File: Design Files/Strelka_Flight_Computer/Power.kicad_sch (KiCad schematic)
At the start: 12 parts

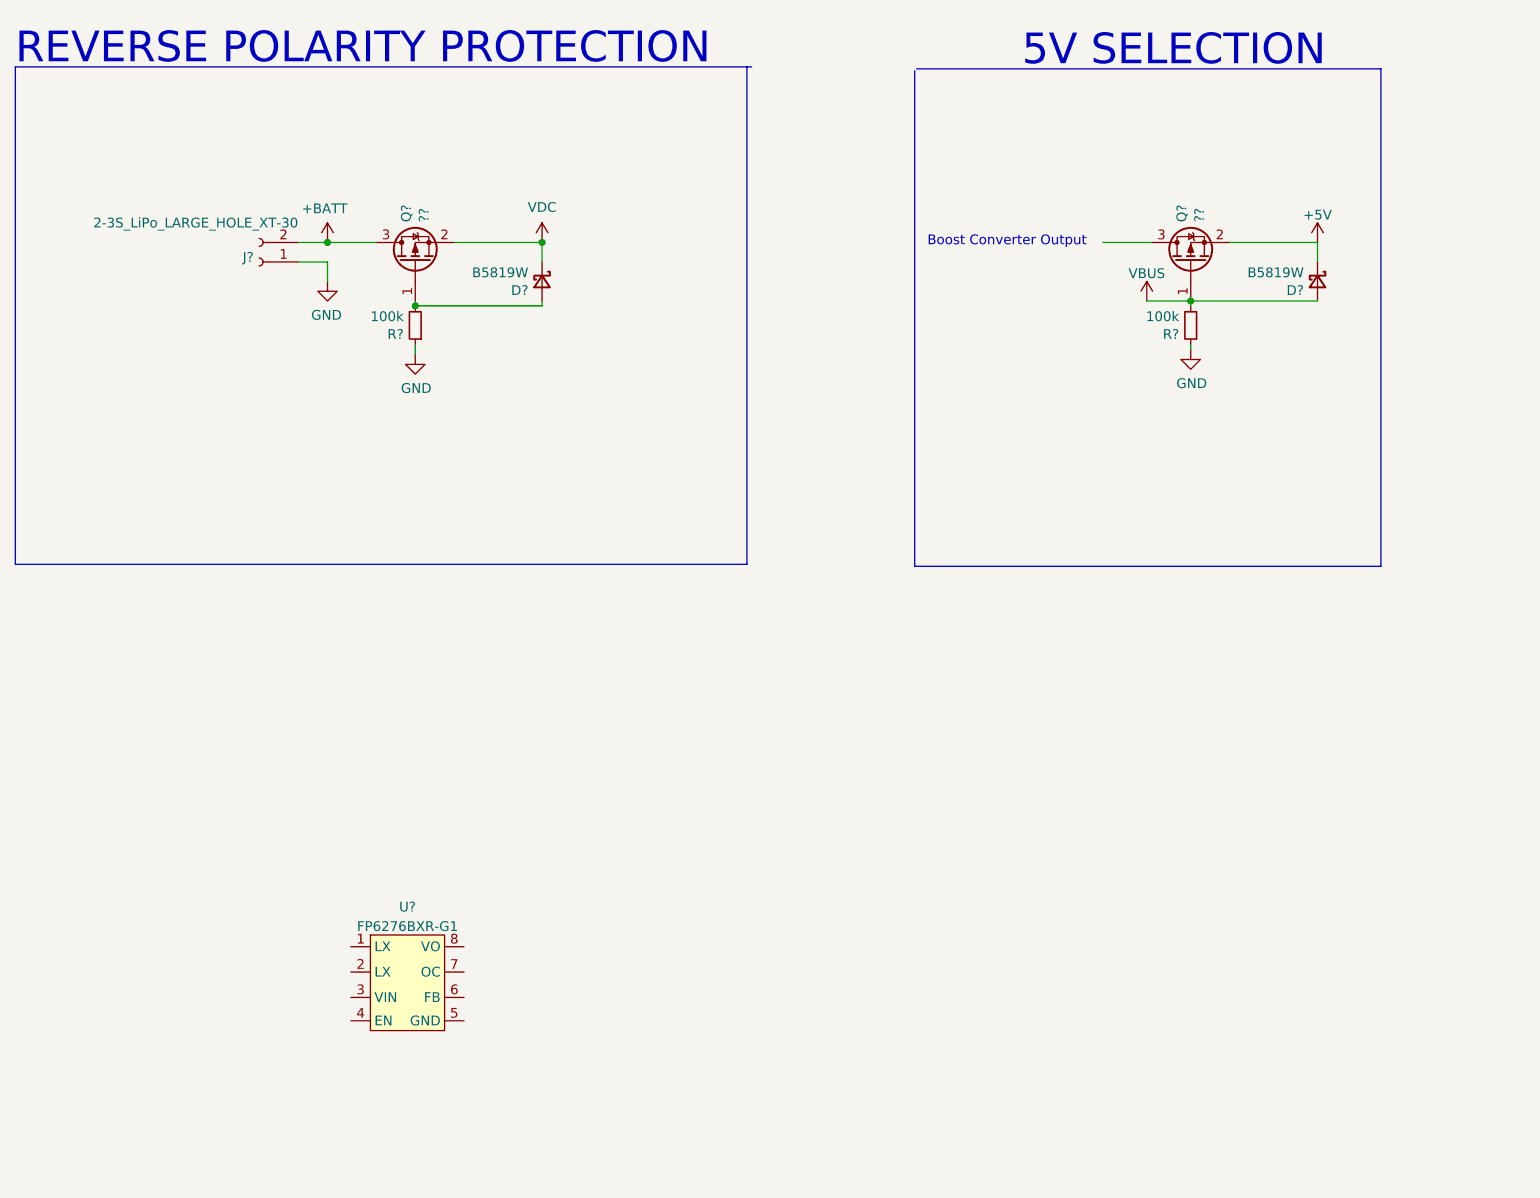
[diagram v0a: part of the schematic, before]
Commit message: Added boost converter
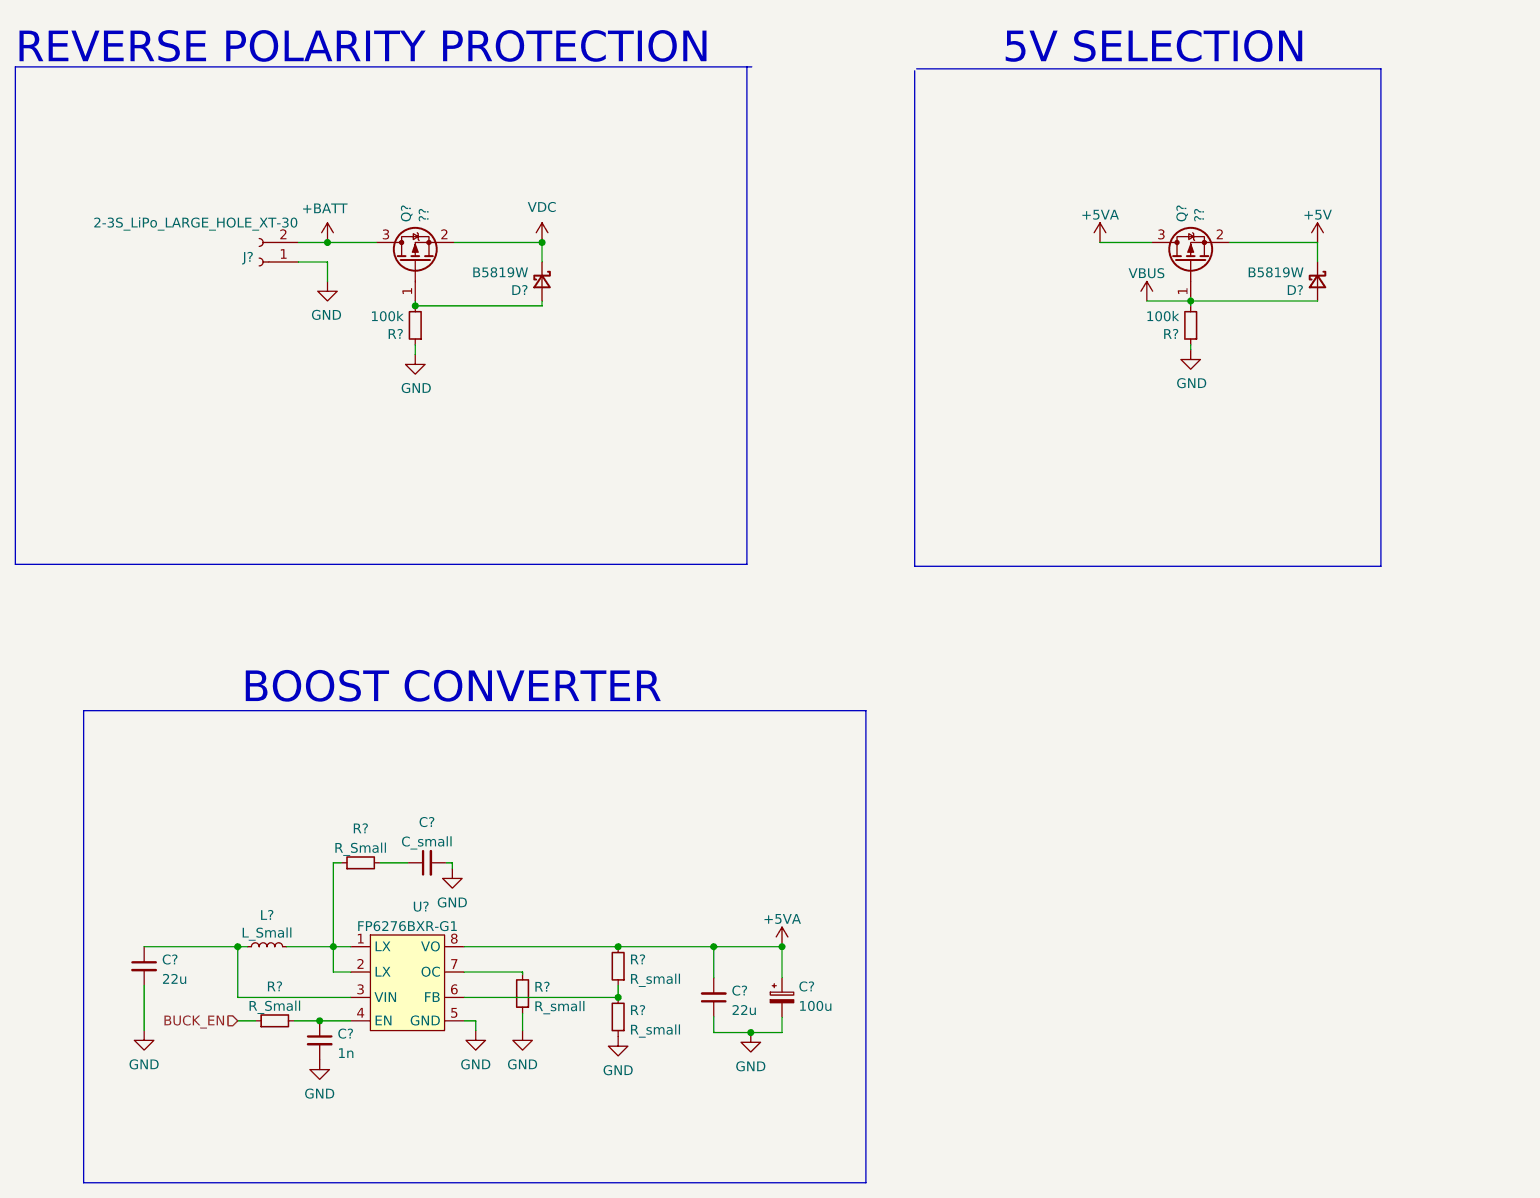
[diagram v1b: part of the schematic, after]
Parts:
- added C? (x2): 22u, symbol Device:C_Small
- added C?: 100u, symbol Device:C_Polarized_Small
- added C?: C_small, symbol Device:C_Small
- added C?: 1n, symbol Device:C_Small
- added L?: L_Small, symbol Device:L_Small
- added R? (x3): R_small, symbol Device:R_Small
- added R? (x2): R_Small, symbol Device:R_Small
- U?: footprint (none) -> Package_SO:Diodes_PSOP-8; LCSC# (none) -> C82652
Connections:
- net GND: now also U?.5 (GND), C?.1, C?.2, C?.2, C?.2, C?.2, R?.1, R?.1
- net +5VA: now reaches Q?.3 (D)
- net +5VA: now also U?.8 (VO), C?.1, C?.2, R?.2
- net at U?.1 (LX): now also U?.2 (LX), L?.2, R?.1
- net at U?.3 (VIN): now also C?.1, L?.1
- net at U?.4 (EN): now also C?.1, R?.2
- net at U?.6 (FB): now also R?.1, R?.2
- net at U?.7 (OC): now also R?.2
- new net: C?.1, R?.2
- new net BUCK_EN: R?.1
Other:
- note added: "BOOST CONVERTER"
- note removed: "Boost Converter Output"

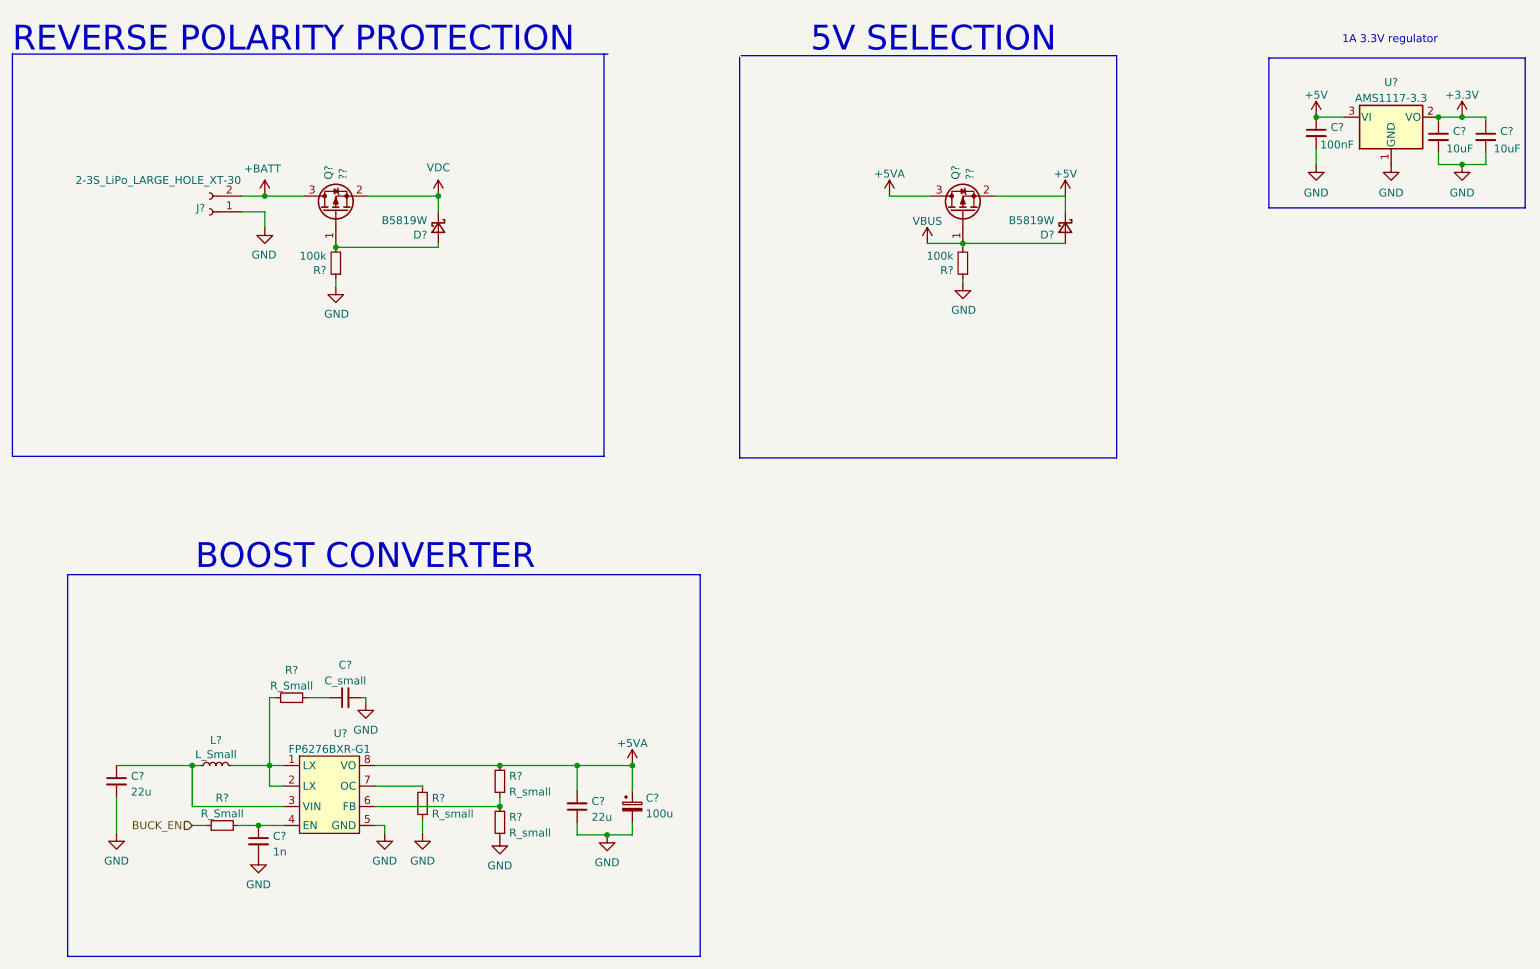
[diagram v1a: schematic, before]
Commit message: Working SPICE sim for ematch continuity circuit
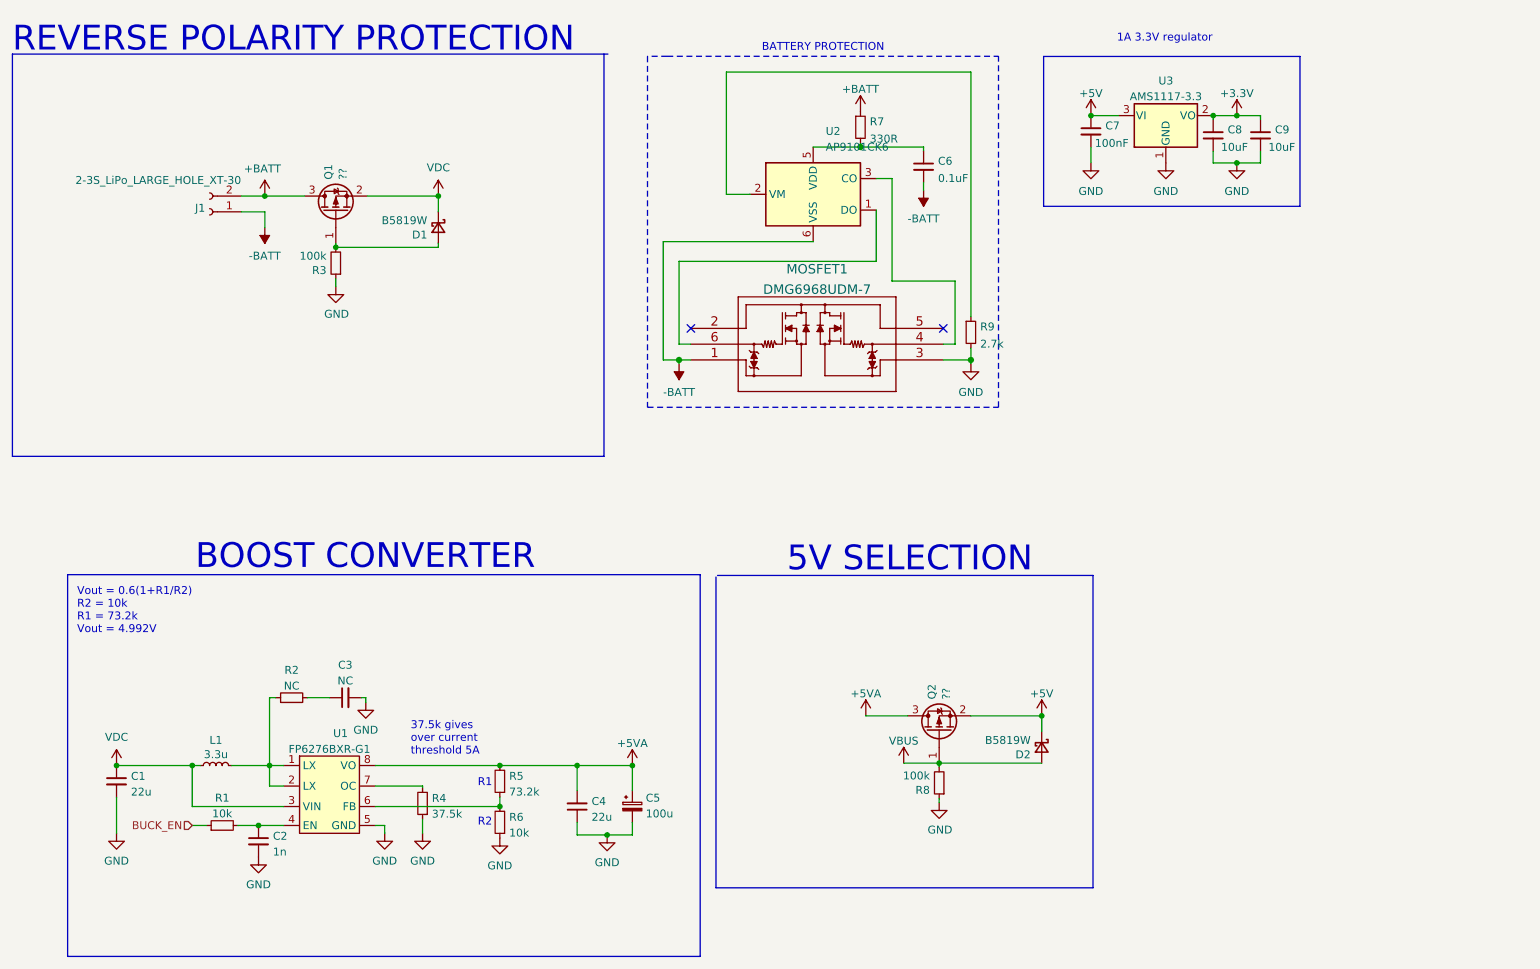
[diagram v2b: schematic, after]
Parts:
- added C6: 0.1uF, Capacitor_SMD:C_0603_1608Metric, symbol Device:C_Small
- added MOSFET1: DMG6968UDM-7, footprints:DMG6968UDM-7, symbol DMG6968UDM-7:DMG6968UDM-7
- added R7: 330R, Resistor_SMD:R_0603_1608Metric, symbol Device:R_Small
- added R9: 2.7k, Resistor_SMD:R_0603_1608Metric, symbol Device:R_Small
- added U2: AP9101CK6, Package_TO_SOT_SMD:SOT-23-6, symbol Battery_Management:AP9101CK6
- C1, C2, C4: renamed from C?; footprint (none) -> Capacitor_SMD:C_0603_1608Metric
- C3: renamed from C?; value C_small -> NC; footprint (none) -> Capacitor_SMD:C_0603_1608Metric
- L1: renamed from L?; value L_Small -> 3.3u; footprint (none) -> Inductor_SMD:L_Vishay_IHLP-2020; LCSC# (none) -> C553993
- R1: renamed from R?; value R_Small -> 10k; footprint (none) -> Resistor_SMD:R_0603_1608Metric
- R2: renamed from R?; value R_Small -> NC; footprint (none) -> Resistor_SMD:R_0603_1608Metric
- R4: renamed from R?; value R_small -> 37.5k; footprint (none) -> Resistor_SMD:R_0603_1608Metric
- R5: renamed from R?; value R_small -> 73.2k; footprint (none) -> Resistor_SMD:R_0603_1608Metric; LCSC# (none) -> C403343
- R6: renamed from R?; value R_small -> 10k; footprint (none) -> Resistor_SMD:R_0603_1608Metric
- gave numbers to parts that had none: 13
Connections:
- net +BATT: now also R7.1
- net GND: now also MOSFET1.3 (S2), R9.2; no longer J1.1 (Pin_1)
- net VDC: now also C1.1, L1.1, U1.3 (VIN)
- new net: MOSFET1.4 (G2), U2.3 (CO)
- new net: MOSFET1.6 (G1), U2.1 (DO)
- new net: R9.1, U2.2 (VM)
- new net: C6.1, R7.2, U2.5 (VDD)
- new net -BATT: C6.2, J1.1 (Pin_1), MOSFET1.1 (S1), U2.6 (VSS)
- no-connect marks 0 -> 2
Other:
- note added: "37.5k gives over current threshold 5A"
- note added: "BATTERY PROTECTION"
- note added: "R1"
- note added: "R2"
- note added: "Vout = 0.6(1+R1/R2) R2 = 10k R1 = 73.2k Vout = 4.992V"
- moved on the sheet: C7, C8, C9, D2, Q2, R8, U3
